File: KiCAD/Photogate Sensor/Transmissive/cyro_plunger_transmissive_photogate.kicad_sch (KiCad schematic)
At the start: 16 parts, among them J1 USB_B_Micro, U1 Opamp_Dual, U2 CH340C, U4 3.8V LDO, U5 AD5242BRUZ1M

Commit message: More revisions
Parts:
- removed U4: 3.8V LDO, Package_TO_SOT_SMD:SOT-23-5, symbol custom:LDO
- added C6, C7: 100nF, Capacitor_SMD:C_0805_2012Metric, symbol Device:C_Small
- added D4, D5, D6: D_Schottky, Diode_SMD:D_SOD-323, symbol Device:D_Schottky
- added J2: UPDI socket, Connector_PinSocket_2.54mm:PinSocket_1x06_P2.54mm_Vertical_SMD_Pin1Right, symbol Connector:Conn_01x06_Socket
- added Q1: Q_NMOS_GSD, Package_TO_SOT_SMD:SOT-23-3, symbol Device:Q_NMOS_GSD
- added R2: 100, Resistor_SMD:R_1206_3216Metric, symbol Device:R
- added R3: 200k, Resistor_SMD:R_0805_2012Metric, symbol Device:R
- added RN1: 50k, Resistor_SMD:R_Array_Convex_4x0603, symbol Device:R_Pack04
- added TP1, TP2, TP3, TP4, TP5, TP6: TestPoint, TestPoint:TestPoint_Pad_D3.0mm, symbol Connector:TestPoint
- added U4: 5V LDO, Package_TO_SOT_SMD:SOT-223-3_TabPin2, symbol Regulator_Linear:AZ1084-5.0
- C4: Part CL21B105KBFNFNE -> CL21B105KBFNNNE
- C5: value 100nF -> 4.7µF; Manufacturer YAGEO -> Samsung Electro-Mechanics; Part CC0805KRX7R9BB104 -> CL21A475KAQNNNE
- U3: value ~ -> ATTiny1614; footprint (none) -> Package_SO:SOIC-14_3.9x8.7mm_P1.27mm; Manufacturer (none) -> Microchip Technology; Part (none) -> ATTINY1614-SSNR
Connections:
- net +5V: now also C5.1, D1.2 (A), U1.8 (V+), U5.16 (A2), C6.1, C7.1, D5.1 (K), D6.1 (K), J2.1 (Pin_1), J2.2 (Pin_2), RN1.5 (R4.2), U4.2 (VO); no longer J1.1 (VBUS)
- net GND: now also C6.2, C7.2, D4.1 (K), J2.6 (Pin_6), RN1.8 (R1.2); no longer C4.2, C5.2, U1.3 (+)
- net Photo_output: now also TP1.1
- net W1: now also TP2.1
- net Vled-ref-: now reaches U5.14 (B2)
- net Vled-ref-: now also D4.2 (A), R2.2, R3.2, TP4.1
- net at U1.6 (-): now also Q1.2 (S), R2.1; no longer U5.15 (W2)
- net Vled-ref+: now reaches U1.5 (+)
- net Vled-ref+: now also U5.15 (W2), R3.1, TP3.1
- net at U1.7: now also Q1.1 (G)
- net Therm3: now reaches U3.11 (8/MOSI/PA1)
- net Therm2: now reaches U3.12 (9/MISO/PA2)
- net Therm1: now reaches U3.13 (10~/SCK/PA3)
- net Heater1: now reaches U3.2 (0~/PA4)
- net Heater2: now reaches U3.3 (1~/PA5)
- net Heater3: now reaches U3.7 (5~/PB2)
- net at D1.1 (K): now also D6.2 (A), Q1.3 (D)
- net Rx: now reaches D3.2 (A), R1.1, U2.3 (RXI)
- net Rx: now also J2.5 (Pin_5)
- net Tx: now reaches D3.1 (K), U2.2 (TXO)
- net Tx: now also J2.4 (Pin_4)
- removed net +3.8V: C4.1, C5.1, U1.8 (V+), U5.16 (A2)
- new net: D5.2 (A), J1.1 (VBUS)
- new net: RN1.1 (R1.1), RN1.2 (R2.1), U1.3 (+)
- new net: C4.2, C5.2, U4.1 (GND)
- new net: RN1.3 (R3.1), RN1.4 (R4.1)
- new net: RN1.6 (R3.2), RN1.7 (R2.2)
- new net +12V: C4.1, U4.3 (VI)
- no-connect marks 11 -> 13
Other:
- note added: "pseudo-log pot https://www.desmos.com/ calculator/bm9tqk4f8c"
- moved on the sheet: C1, C2, C3, D1, D2, D3, J1, R1, U1A, U1B, U1C, U2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

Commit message: Finish draft of schematic, started on board
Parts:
- added D7, D8, D9: D_Schottky, Diode_SMD:D_SOD-323, symbol Device:D_Schottky
- added J1: FFC, symbol Connector:Conn_01x08_Pin
- added J2: FFC Socket, Custom:AMPHENOL_SFW8S-2STE1LF, symbol Connector:Conn_01x08_Socket
- added Q1, Q2, Q3: Q_NMOS_GSD, Package_TO_SOT_SMD:SOT-23-3, symbol Device:Q_NMOS_GSD
- added R1, R2, R3: 47, Custom:RES_SMF5_TYCO_TYC, symbol Device:R
- added RN1: 4.7k, Resistor_SMD:R_Array_Convex_4x1206, symbol Device:R_Pack04
- added TH1, TH2, TH3: Thermistor, Resistor_SMD:R_0805_2012Metric, symbol Device:Thermistor
- J3: renamed from J1; footprint Custom:AMPHENOL_10118193-0001LF -> Custom:CUI_UJ2-MIBH-G-SMT-TR; Manufacturer Amphenol ICC (FCI) -> Same Sky (Formerly CUI Devices); Part 10118193-0001LF -> UJ2-MIBH-G-SMT-TR
- RN2: renamed from RN1; value 50k -> 4.7k; footprint Resistor_SMD:R_Array_Convex_4x0603 -> Resistor_SMD:R_Array_Convex_4x1206; Manufacturer Vishay Beyschlag/Draloric/BC Components -> YAGEO; Part ACASA5002S5002P1AT -> YC324-FK-074K7L
- U3: renamed from U5; footprint RU_16_ADI -> Custom:AD5242BRUZ1M
- renumbered C4 to C1, C5 to C2, C7 to C3, C3 to C4, C6 to C5, C1 to C6, C2 to C7, D6 to D2, D2 to D3, D3 to D5, D5 to D6, J2 to J4, Q1 to Q4, R3 to R4, R2 to R5, R1 to R6, U4 to U1, U1 to U2, U3 to U4, U2 to U5
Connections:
- net +12V: now also D7.1 (K), D8.1 (K), D9.1 (K), J2.1 (Pin_1), J2.3 (Pin_3), J2.5 (Pin_5), R1.1, R2.1, R3.1
- net +5V: now also RN1.5 (R4.2), RN1.6 (R3.2), RN1.7 (R2.2)
- net Comp Out: now also J2.7 (Pin_7)
- net GND: now also J2.2 (Pin_2), J2.4 (Pin_4), J2.6 (Pin_6), J2.8 (Pin_8), Q1.2 (S), Q2.2 (S), Q3.2 (S), TH1.1, TH2.1, TH3.1
- net Heater1: now also Q1.1 (G)
- net Heater2: now also Q2.1 (G)
- net Heater3: now also Q3.1 (G)
- net Therm1: now also RN1.4 (R4.1), TH1.2, TH2.2, TH3.2
- net Therm2: now also RN1.3 (R3.1)
- net Therm3: now also RN1.2 (R2.1)
- new net: D8.2 (A), Q2.3 (D), R2.2
- new net: D9.2 (A), Q3.3 (D), R3.2
- new net: D7.2 (A), Q1.3 (D), R1.2
- no-connect marks 13 -> 23
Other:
- note added: "3 Watt Heaters and Thermistors"
- note added: "5V Voltage Supply"
- note added: "Cables and Hardware"
- note added: "LED and Photodiode"
- note added: "Microcontroller"
- note added: "Test Pads"
- note added: "USB->UPDI Programming Interface"
- moved on the sheet: C1, C2, C3, C4, C5, C6, C7, D1, D2, D3, D4, D5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

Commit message: Analog and digital circuits mostly connected
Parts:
- R3: footprint Custom:RES_SMF5_TYCO_TYC -> Custom:RES_3550_TEC; Part SMW547RJT -> 355047RJT
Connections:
- net +12V: no longer J2.1 (Pin_1)
- net +5V: now also RN1.8 (R1.2); no longer J4.1 (Pin_1), J4.2 (Pin_2), RN1.5 (R4.2)
- net GND: now also C1.2, C2.2, U1.1 (GND); no longer J2.2 (Pin_2), J2.8 (Pin_8)
- net Heater1: now also U4.7 (5~/PB2); no longer U4.2 (0~/PA4)
- net Heater3: now also U4.2 (0~/PA4); no longer U4.7 (5~/PB2)
- net Therm1: now also RN1.3 (R3.1), U4.11 (8/MOSI/PA1); no longer RN1.4 (R4.1), TH2.2, TH3.2, U4.13 (10~/SCK/PA3)
- net Therm2: now also RN1.2 (R2.1), TH2.2; no longer RN1.3 (R3.1)
- net Therm3: now also RN1.1 (R1.1), TH3.2, U4.13 (10~/SCK/PA3); no longer RN1.2 (R2.1), U4.11 (8/MOSI/PA1)
- net Vled-ref+: no longer TP3.1
- net Vled-ref-: no longer TP4.1
- net Vusb: now reaches D6.2 (A), J3.1 (VBUS)
- net Vusb: now also J2.8 (Pin_8), J4.1 (Pin_1), J4.2 (Pin_2)
- net D-: now reaches J3.2 (D-), U5.6 (UD-)
- net D-: now also J2.2 (Pin_2)
- net D+: now reaches J3.3 (D+), U5.5 (UD+)
- net D+: now also J2.1 (Pin_1)
- net LED Isense: now reaches Q4.2 (S), R5.1, U2.6 (-)

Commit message: Add RC filter and I2C breakout - passes DRC
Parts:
- removed TP2, TP3, TP4, TP5, TP6: TestPoint, TestPoint:TestPoint_Pad_D3.0mm, symbol Connector:TestPoint
- added C8: 100nF, Capacitor_SMD:C_0805_2012Metric, symbol Device:C_Small
- added J6: Conn_01x03_Socket, Custom:GCT_BG300-03-X-X-A_REVC, symbol Connector:Conn_01x03_Socket
- added R7: 470, Resistor_SMD:R_0805_2012Metric, symbol Device:R
- D1: footprint LED_THT:LED_D5.0mm_Horizontal_O1.27mm_Z9.0mm -> Custom:Solder pads
- D3: footprint (none) -> Custom:Solder pads
- R6: Manufacturer TE Connectivity Passive Product -> Panasonic Electronic Components; Part CRGCQ0805J470R -> ERA-6AEB471V
- TP1: footprint TestPoint:TestPoint_Pad_D3.0mm -> Custom:1x Solder pads
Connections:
- net GND: now also R4.2, U3.14 (B2), C8.1, J6.3 (Pin_3)
- net Photo_output: now also R7.1; no longer U4.5 (3/PA7)
- net SCL: now also U4.9 (7~/SCL/PB0), J6.1 (Pin_1); no longer U4.8 (6~/SDA/PB1)
- net SDA: now also U4.8 (6~/SDA/PB1), J6.2 (Pin_2); no longer U4.9 (7~/SCL/PB0)
- net Vled-ref-: no longer names the net of D4.2 (A), R5.2
- net Vled-ref-: no longer R4.2, U3.14 (B2)
- new net Filtered_output: C8.2, R7.2, U4.5 (3/PA7)
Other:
- note added: "Optional RC Filter"

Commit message: Add digipot bypass - upgrade to moisture resistance when possible
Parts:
- added R8: 2M, Resistor_SMD:R_0805_2012Metric, symbol Device:R
- added RN3: 4.7k, Resistor_SMD:R_Array_Convex_4x1206, symbol Device:R_Pack04
- C1: value 1µF -> 4.7µF; Manufacturer Samsung Electro-Mechanics -> Murata Electronics; Part CL21B105KBFNNNE -> GRT21BR61H475KE13L
- C2: Manufacturer Samsung Electro-Mechanics -> Murata Electronics; Part CL21A475KAQNNNE -> GRT21BR61H475KE13L
- C3, C4, C5, C6, C7, C8: Manufacturer YAGEO -> Walsin Technology Corporation; Part CC0805KRX7R9BB104 -> MT21B104K500CT
- J6: footprint Custom:GCT_BG300-03-X-X-A_REVC -> Connector_PinSocket_2.54mm:PinSocket_1x03_P2.54mm_Vertical_SMD_Pin1Right; Manufacturer GCT -> Sullins Connector Solutions; Part BG300-03-A-L-A -> NPPC031KFXC-RC
- R4: Manufacturer Panasonic Electronic Components -> TE Connectivity Passive Product; Part ERA-6AEB204V -> CPF-A-0805B200KE
- R5: Manufacturer Stackpole Electronics Inc -> YAGEO; Part RNCP1206FTD100R -> RP1206BRD07100RL
- R6, R7: Manufacturer Panasonic Electronic Components -> YAGEO; Part ERA-6AEB471V -> RP0805FRE07470RL
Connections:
- net +5V: now also C3.2, C4.1, C5.2, C6.2, RN3.1 (R1.1), RN3.2 (R2.1), RN3.3 (R3.1), RN3.4 (R4.1); no longer C3.1, C4.2, C5.1, C6.1
- net GND: now also C3.1, C4.2, C5.1, C6.1, C7.1; no longer C3.2, C4.1, C5.2, C6.2, C7.2
- net SCL: now also RN3.7 (R2.2), RN3.8 (R1.2)
- net SDA: now also RN3.5 (R4.2), RN3.6 (R3.2)
- net at U5.4 (V3): now also C7.2; no longer C7.1
- net Photo_output renamed Amplifier_output
- net Amplifier_output: now also U3.3 (W1), R8.1; no longer U3.4 (B1)
- net W1 renamed Photo_current
- net Photo_current: now also U3.4 (B1), R8.2; no longer U3.3 (W1)
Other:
- note added: "Constant Current Source"
- note added: "I2C Connector"
- note added: "I2C Pullup"
- note added: "Optional digipot bypass resistor"
- note added: "Transimpedance Amplifier"
- moved on the sheet: D3, RN2, U2A

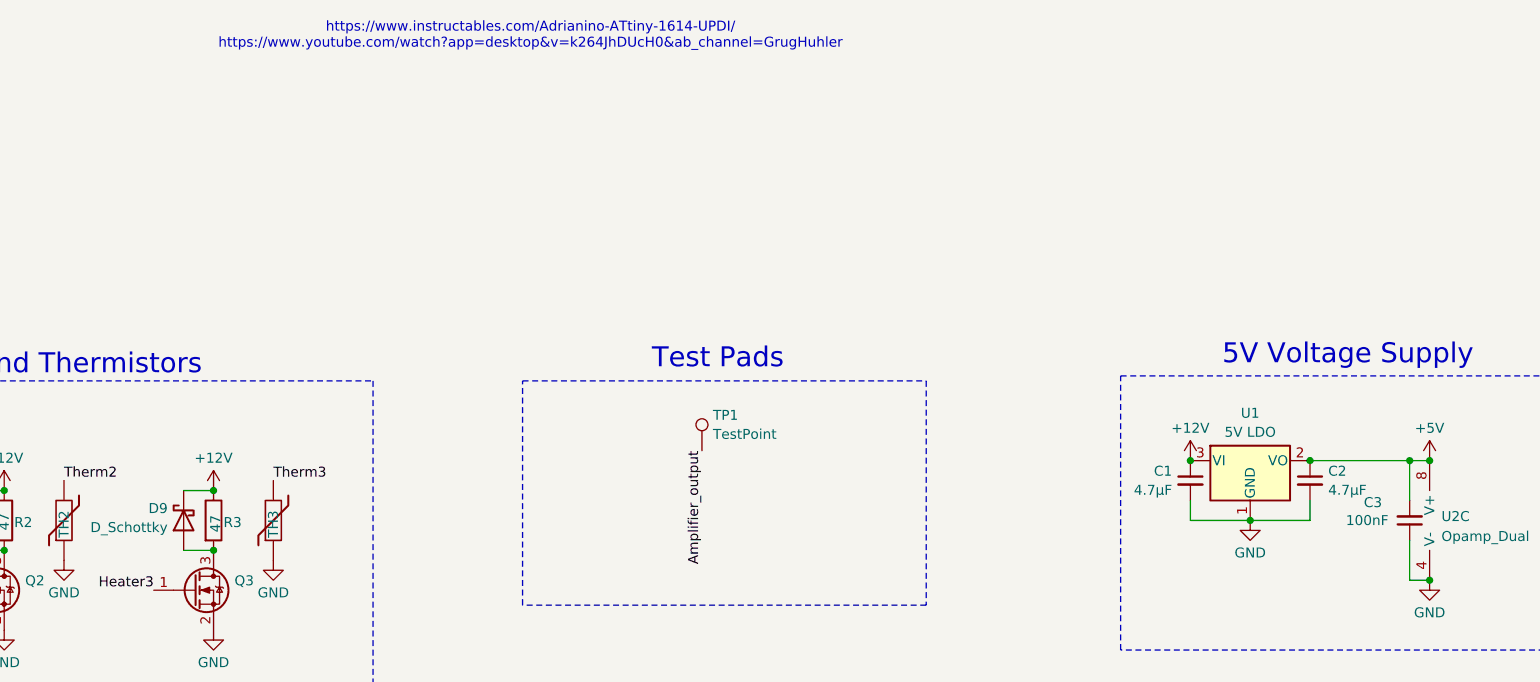
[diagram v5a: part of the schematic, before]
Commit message: A license info to board
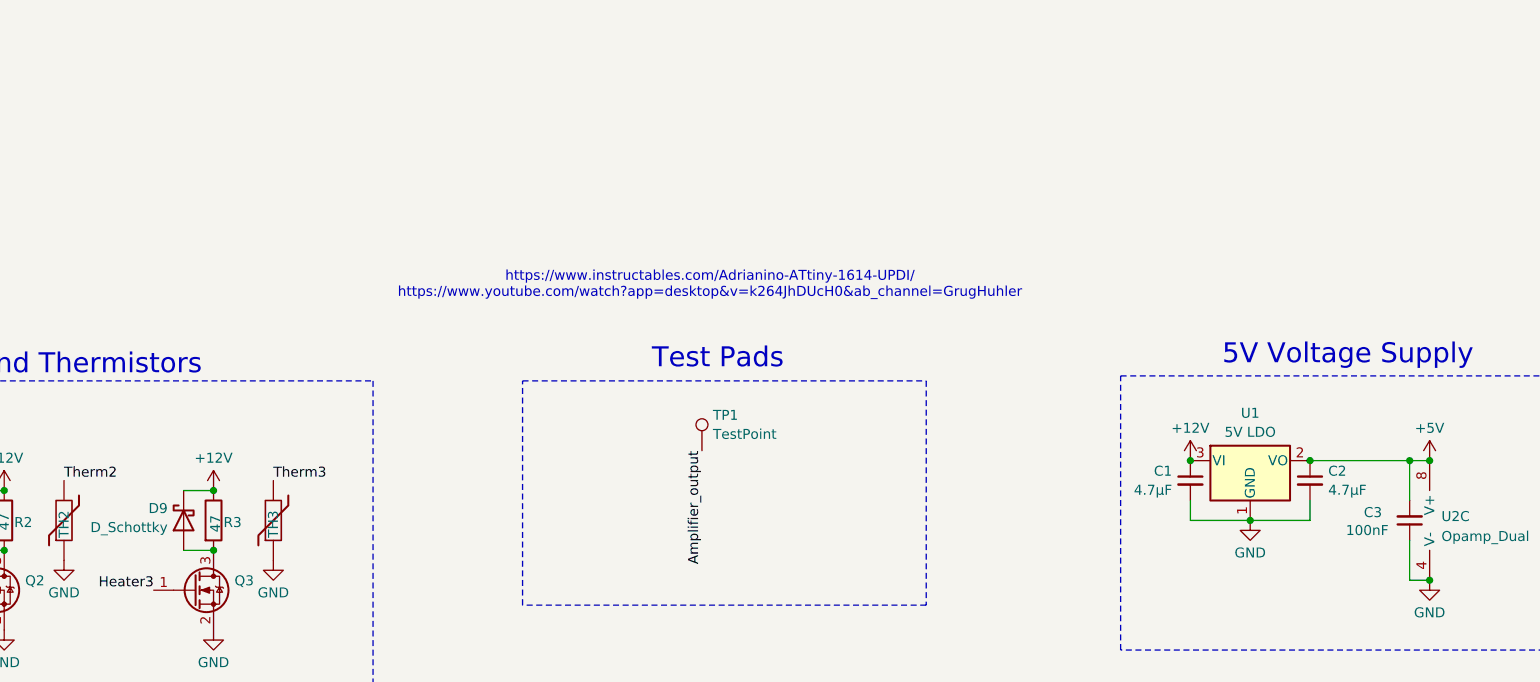
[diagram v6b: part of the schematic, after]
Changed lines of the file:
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@@
 	(text "https://www.instructables.com/Adrianino-ATtiny-1614-UPDI/\nhttps://www.youtube.com/watch?app=desktop&v=k264JhDUcH0&ab_channel=GrugHuhler"
 		(exclude_from_sim no)
-		(at 130.556 -24.892 0)
+		(at 153.416 6.858 0)
 		(effects
 			(font
@@
 		(dnp no)
 		(property "Reference" "C3"
-			(at 236.728 34.544 0)
+			(at 236.728 35.814 0)
 			(effects
 				(font
@@
 		)
 		(property "Value" "100nF"
-			(at 234.442 36.83 0)
+			(at 234.442 38.1 0)
 			(effects
 				(font
